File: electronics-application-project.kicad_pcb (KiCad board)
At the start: 2 copper layers, 52 x 32.5 mm, 42 parts, among them J1 Conn_02x03_Odd_Even, U1 W5500, U2 ARJM11C7-114-BA-EW2, U3 LM2574-3.3YN, U4 ATTINY85-20SU, Y2 ABLS7M2-25.000MHZ-D-2Y-T

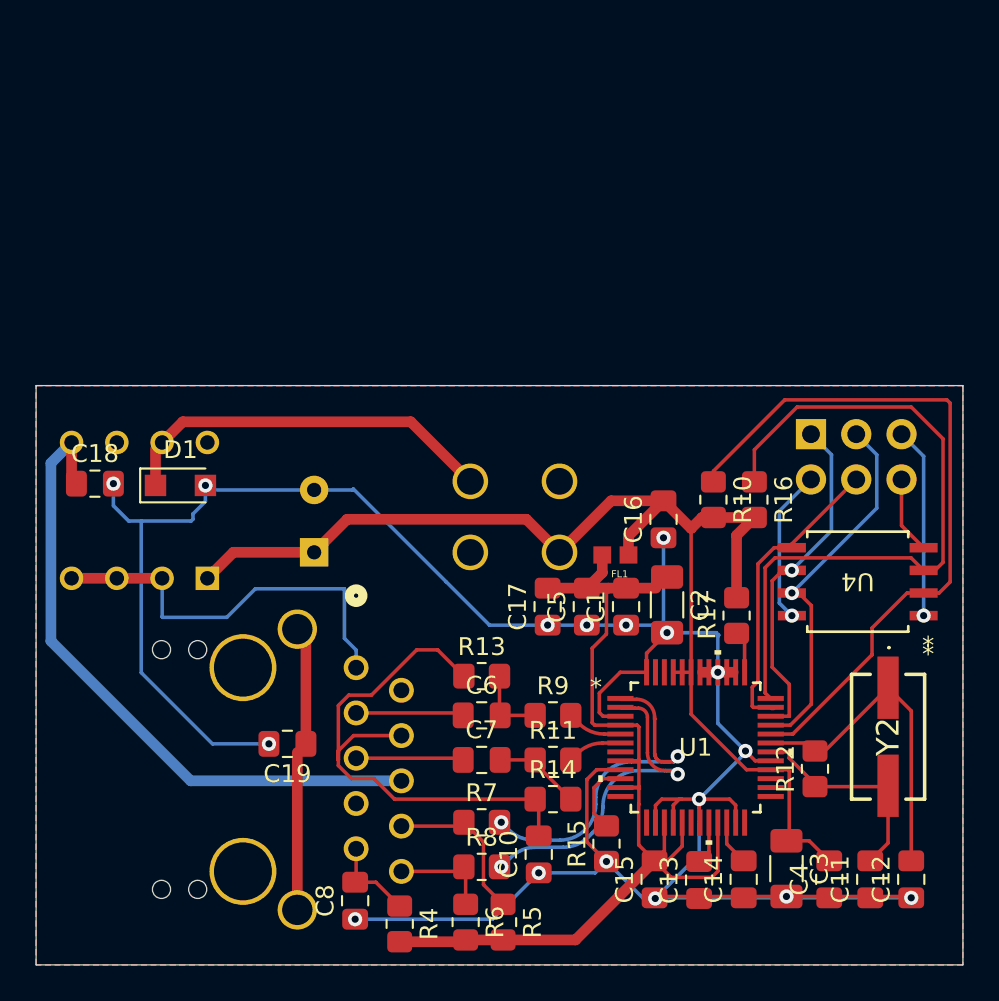
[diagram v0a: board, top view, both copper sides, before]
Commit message: add ethernet leds; change power supply capacitors; change attiny85 pin connections;
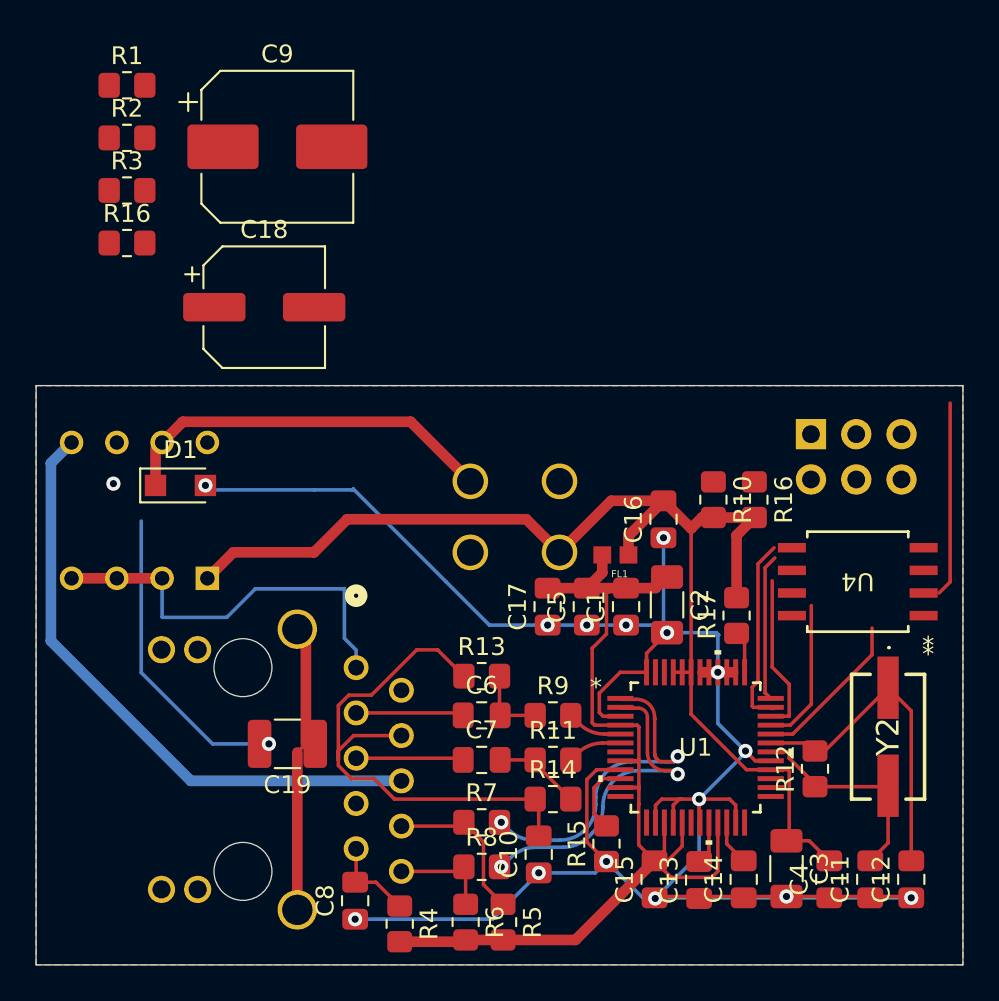
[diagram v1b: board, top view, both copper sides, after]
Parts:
- added R1: 4.7K, Resistor_SMD:R_0805_2012Metric_Pad1.20x1.40mm_HandSolder, F.Cu at (114.6, 54.1)
- added R16: 4.7K, Resistor_SMD:R_0805_2012Metric_Pad1.20x1.40mm_HandSolder, F.Cu at (114.6, 63.0)
- added R2: 330, Resistor_SMD:R_0805_2012Metric_Pad1.20x1.40mm_HandSolder, F.Cu at (114.6, 57.1)
- added R3: 330, Resistor_SMD:R_0805_2012Metric_Pad1.20x1.40mm_HandSolder, F.Cu at (114.6, 60.0)
- C18: footprint Capacitor_SMD:C_0805_2012Metric_Pad1.18x1.45mm_HandSolder -> Capacitor_SMD:CP_Elec_6.3x5.4
- C19: footprint Capacitor_SMD:C_0805_2012Metric_Pad1.18x1.45mm_HandSolder -> Capacitor_SMD:C_1210_3225Metric_Pad1.33x2.70mm_HandSolder
- C9: footprint Capacitor_THT:CP_Radial_D8.0mm_P3.50mm -> Capacitor_SMD:CP_Elec_8x6.2; moved to F.Cu
- U2: footprint Imported:ARJM11C7-114-BA-EW2_ABR -> Imported:ARJM11C7-114-BA-EW2_ABR-fixed
- moved C9 22.8 mm to (123.0, 57.6), turned to 0 degrees
- moved C18 13.7 mm to (122.3, 66.6)
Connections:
- J1 pad 1: /MISO -> /SCLK
- J1 pad 3: /SCLK -> Net-(J1-Pin_3)
- J1 pad 4: /MOSI -> /MISO
- U4 pad 2: /SCSn -> /MOSI
- U4 pad 3: /INTn -> /SCSn
- U4 pad 5: /MOSI -> /MISO
- U4 pad 6: /MISO -> /SCLK
- U4 pad 7: /SCLK -> Net-(J1-Pin_3)
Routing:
- net /SCSn: track 40.1 -> 9.03 mm
- net /INTn: track 39.2 -> 8.24 mm
- net /SCLK: track 21.0 -> 8.30 mm, vias 1 -> 0
- net Net-(J1-Pin_5): track 10.7 -> 0.00 mm, vias 1 -> 0
- net /MISO: track 19.4 -> 9.03 mm, vias 1 -> 0
- net Net-(J1-Pin_2): track 8.67 -> 0.00 mm, vias 1 -> 0
- net GND: track 180.0 -> 171.7 mm
- net /MOSI: track 17.0 -> 21.6 mm
- net Net-(J1-Pin_6): track 4.34 -> 0.00 mm
- net Net-(U2-VC2+): track 37.0 -> 34.5 mm

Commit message: start over
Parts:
- removed the R16 at (114.6, 63.0)
- removed the R16 at (149.8, 77.4)
- added R16: 4.7K, Resistor_SMD:R_0805_2012Metric_Pad1.20x1.40mm_HandSolder, F.Cu at (120.5, 92.7)
- C18, C9, D1: moved to B.Cu
- moved U3 45.4 mm to (161.3, 98.6), turned to 180 degrees
- moved C4 41.5 mm to (131.7, 63.7), turned to 0 degrees
- moved C8 40.2 mm to (136.5, 60.7), turned to 0 degrees
- moved C14 38.8 mm to (141.3, 60.7), turned to 0 degrees
- moved R12 37.9 mm to (115.8, 98.6), turned to 0 degrees
- moved C11 37.6 mm to (136.5, 66.7), turned to 0 degrees
- moved C12 36.4 mm to (136.5, 69.7), turned to 0 degrees
- moved R10 35.2 mm to (115.8, 92.7), turned to 0 degrees
- moved C15 35.1 mm to (141.3, 63.7), turned to 0 degrees
- moved C10 33.6 mm to (136.5, 63.7), turned to 0 degrees
- moved C1 31.4 mm to (148.7, 52.6), turned to 0 degrees
- moved R17 30.6 mm to (120.5, 95.6), turned to 0 degrees
- moved L1 30.6 mm to (122.2, 55.6)
- moved R1 29.9 mm to (111.0, 83.8)
- moved R2 29.9 mm to (111.0, 86.8)
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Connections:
- J1 pad 3: Net-(J1-Pin_3) -> /INTn
- R1 pad 1: Net-(J1-Pin_3) -> /INTn
- U4 pad 7: Net-(J1-Pin_3) -> /INTn
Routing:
- net GND: track 171.7 -> 0.00 mm, vias 17 -> 0
- net 3.3V_D: track 68.8 -> 0.00 mm
- net 3.3V_A: track 60.6 -> 0.00 mm
- net Net-(U2-VC2+): track 34.5 -> 0.00 mm
- net Net-(U2-RCT): track 31.2 -> 0.00 mm
- net Net-(D1-K): track 21.7 -> 0.00 mm
- net /MOSI: track 21.6 -> 0.00 mm
- net Net-(U1-TXN): track 19.1 -> 0.00 mm, vias 2 -> 0
- net Net-(U1-TXP): track 18.7 -> 0.00 mm, vias 2 -> 0
- net /XO: track 18.5 -> 0.00 mm
- net Net-(C19-Pad1): track 17.7 -> 0.00 mm
- net /XI: track 12.3 -> 0.00 mm
- net Net-(U2-TD-): track 9.10 -> 0.00 mm
- net /MISO: track 9.03 -> 0.00 mm
- net /SCSn: track 9.03 -> 0.00 mm
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- removed copper zone on B.Cu, net GND
- removed copper zone on F.Cu, net GND
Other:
- board outline removed

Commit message: pcb progress
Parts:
- R1, R10, R16, R17, R7, R8: moved to B.Cu
- moved R10 80.0 mm to (195.5, 86.0), turned to 90 degrees
- moved C4 77.7 mm to (191.0, 114.0), turned to 90 degrees
- moved C11 75.6 mm to (195.5, 114.0), turned to 90 degrees
- moved C12 75.3 mm to (197.5, 114.0), turned to 90 degrees
- moved R12 75.1 mm to (190.0, 110.0), turned to 90 degrees
- moved R1 75.0 mm to (186.0, 86.0), turned to 90 degrees
- moved C14 73.5 mm to (185.5, 119.5), turned to 90 degrees
- moved R16 70.3 mm to (190.5, 86.0), turned to 90 degrees
- moved C15 67.6 mm to (179.5, 119.5), turned to 90 degrees
- moved Y2 65.3 mm to (194.0, 106.5), turned to -90 degrees
- moved C13 65.2 mm to (182.0, 119.5), turned to 90 degrees
- moved R17 63.2 mm to (183.5, 101.0), turned to 90 degrees
- moved R7 59.4 mm to (170.0, 108.0)
- moved R8 59.0 mm to (170.0, 110.0)
- moved C5 58.7 mm to (177.0, 104.0), turned to 90 degrees
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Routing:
- net GND: track 0.00 -> 44.4 mm, vias 0 -> 1
- net /INTn: track 0.00 -> 36.5 mm
- net /SCSn: track 0.00 -> 33.0 mm, vias 0 -> 1
- net 3.3V_A: track 0.00 -> 31.0 mm
- net /SCLK: track 0.00 -> 25.9 mm
- net /MISO: track 0.00 -> 25.3 mm
- net /XO: track 0.00 -> 23.4 mm
- net /MOSI: track 0.00 -> 19.4 mm, vias 0 -> 2
- net Net-(J1-Pin_5): track 0.00 -> 18.6 mm
- net Net-(J1-Pin_2): track 0.00 -> 15.1 mm
- net 3.3V_D: track 0.00 -> 14.3 mm
- net /XI: track 0.00 -> 13.7 mm
- net Net-(U1-TXP): track 0.00 -> 6.50 mm, vias 0 -> 1
- net Net-(U1-TXN): track 0.00 -> 6.50 mm, vias 0 -> 1
- net Net-(U1-RXP): track 0.00 -> 6.00 mm
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
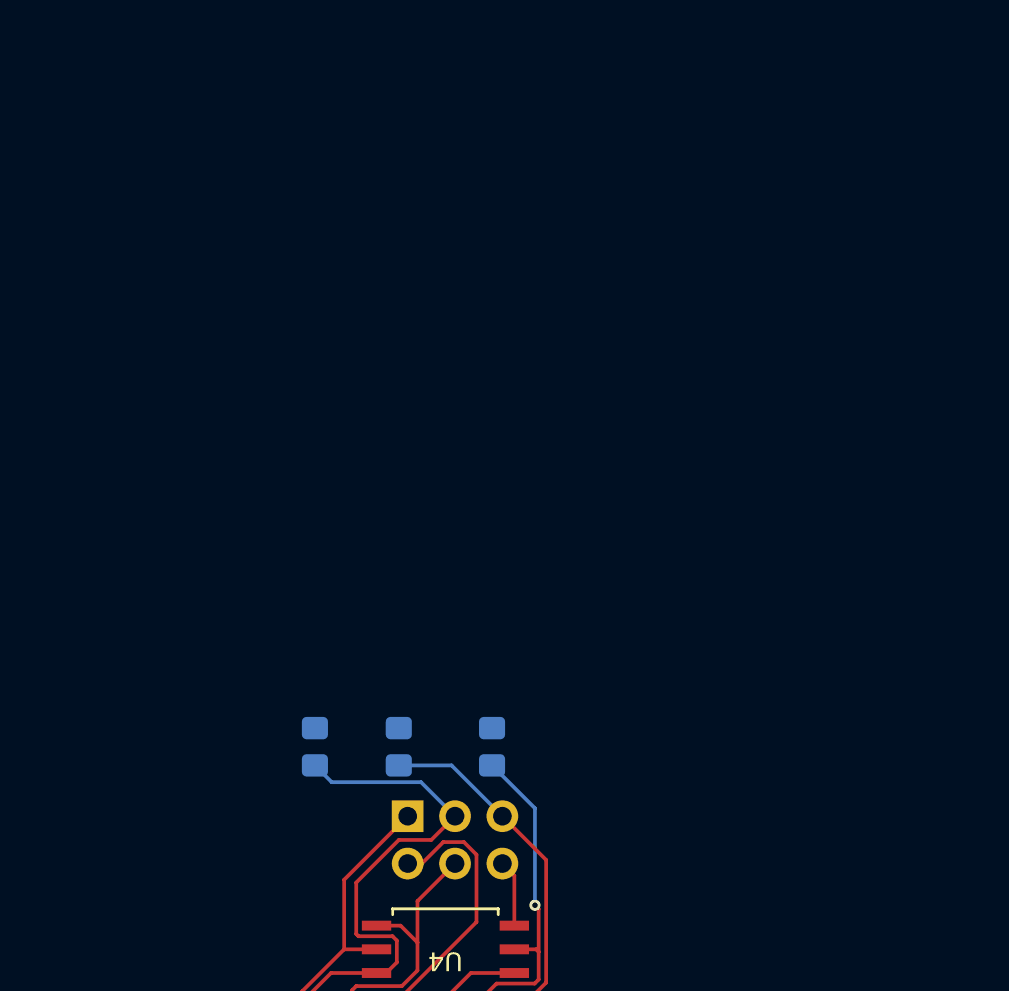
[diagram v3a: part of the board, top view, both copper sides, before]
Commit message: add NAND gates and a pin header for UART and PWM; add buzzer; add pin header for GND and 3.3V_D; expand ATtiny85 pin header to all pins; join W5500 RST and ATtiny85 RST and add a pin header for the net;
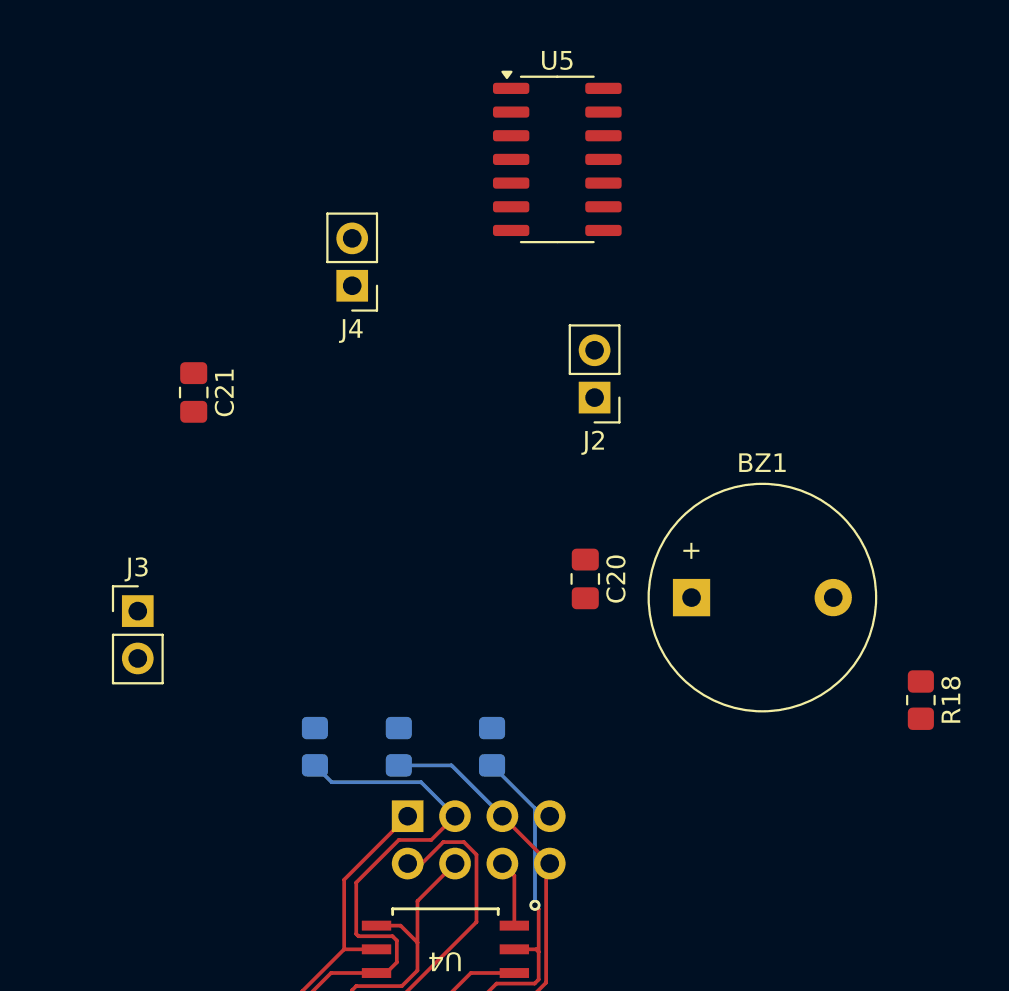
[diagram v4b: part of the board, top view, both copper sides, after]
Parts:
- added BZ1: Buzzer, Buzzer_Beeper:Buzzer_12x9.5RM7.6, F.Cu at (206.2, 78.0)
- added C20: C_Polarized, Capacitor_SMD:C_0805_2012Metric_Pad1.18x1.45mm_HandSolder, F.Cu at (200.5, 77.0)
- added C21: 100nF, Capacitor_SMD:C_0805_2012Metric_Pad1.18x1.45mm_HandSolder, F.Cu at (179.5, 67.0)
- added J2: Conn_01x02_Pin, Connector_PinHeader_2.54mm:PinHeader_1x02_P2.54mm_Vertical, F.Cu at (201.0, 67.3)
- added J3: Conn_01x02_Pin, Connector_PinHeader_2.54mm:PinHeader_1x02_P2.54mm_Vertical, F.Cu at (176.5, 78.7)
- added J4: Conn_01x02_Pin, Connector_PinHeader_2.54mm:PinHeader_1x02_P2.54mm_Vertical, F.Cu at (188.0, 61.3)
- added R18: R, Resistor_SMD:R_0805_2012Metric_Pad1.20x1.40mm_HandSolder, F.Cu at (218.5, 83.5)
- added U5: 74HC00, Package_SO:SO-14_3.9x8.65mm_P1.27mm, F.Cu at (199.0, 54.5)
- J1: footprint Connector_PinHeader_2.54mm:PinHeader_2x03_P2.54mm_Vertical -> Connector_PinHeader_2.54mm:PinHeader_2x04_P2.54mm_Vertical
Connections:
- J1 pad 5: Net-(J1-Pin_5) -> /RSTn
- U4 pad 1: Net-(J1-Pin_5) -> /RSTn

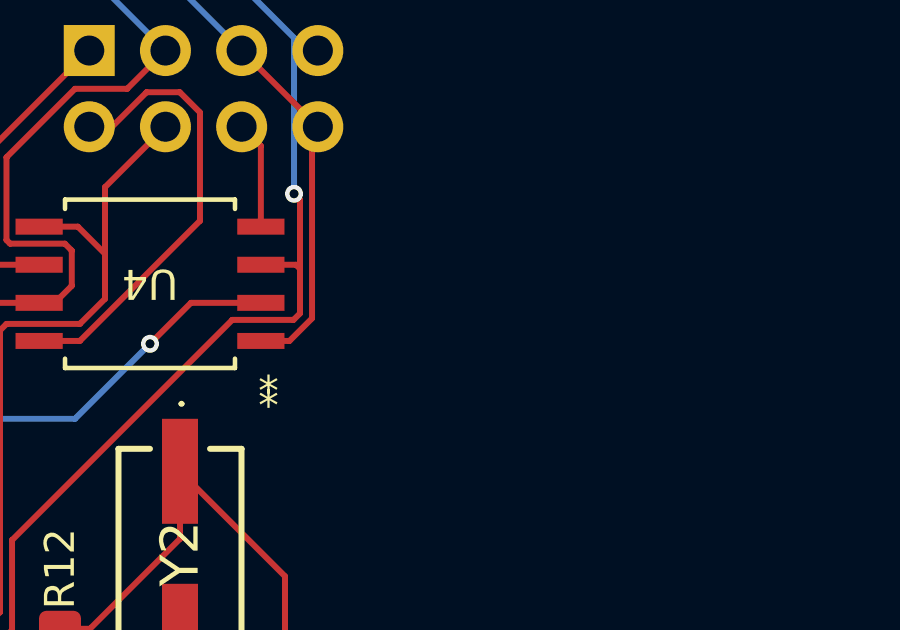
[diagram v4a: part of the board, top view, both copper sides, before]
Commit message: update pcb from schematic
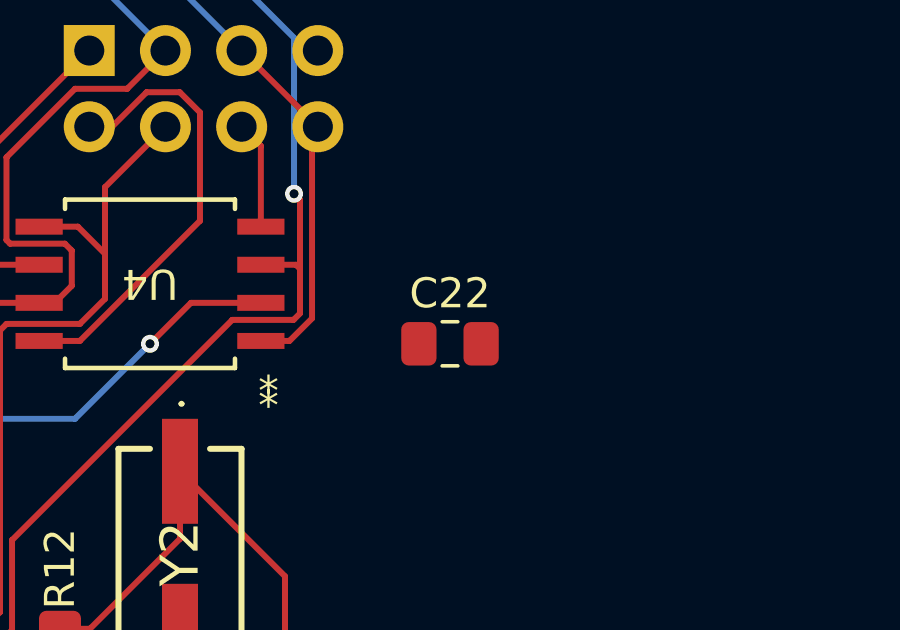
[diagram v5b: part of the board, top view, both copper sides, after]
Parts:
- added C22: C, Capacitor_SMD:C_0805_2012Metric_Pad1.18x1.45mm_HandSolder, F.Cu at (203.0, 99.5)
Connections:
- J1 pad 2: Net-(J1-Pin_2) -> 3.3V_D
- J1 pad 6: Net-(J1-Pin_6) -> GND
- U4 pad 4: Net-(J1-Pin_6) -> GND
- U4 pad 8: Net-(J1-Pin_2) -> 3.3V_D
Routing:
- net Net-(J1-Pin_2): track 15.1 -> 0.00 mm
- net 3.3V_D: track 14.3 -> 29.3 mm
- net GND: track 44.4 -> 48.0 mm
- net Net-(J1-Pin_6): track 3.60 -> 0.00 mm

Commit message: pcb done, but has some errors still
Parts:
- C22, R4, R5, R6: moved to B.Cu
- moved BZ1 61.6 mm to (145.8, 90.0), turned to 180 degrees
- moved C16 59.6 mm to (119.0, 122.0), turned to 90 degrees
- moved C10 58.5 mm to (132.0, 122.0), turned to 90 degrees
- moved C17 55.1 mm to (124.0, 122.0), turned to 90 degrees
- moved U3 52.4 mm to (125.3, 95.3), turned to 90 degrees
- moved R18 50.5 mm to (168.0, 84.5), turned to 0 degrees
- moved J4 46.2 mm to (173.2, 105.0), turned to 90 degrees
- moved U5 45.4 mm to (175.0, 93.0), turned to 180 degrees
- moved C8 45.1 mm to (131.5, 105.5), turned to -90 degrees
- moved C22 43.8 mm to (159.5, 105.0), turned to 90 degrees
- moved R13 41.4 mm to (136.5, 122.0), turned to 90 degrees
- moved R15 41.2 mm to (145.5, 122.5), turned to 90 degrees
- moved R14 40.8 mm to (141.0, 122.0), turned to 90 degrees
- moved L1 40.0 mm to (135.0, 93.5)
- moved D1 35.6 mm to (131.5, 82.0), turned to 0 degrees
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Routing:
- net 3.3V_D: track 29.3 -> 195.2 mm, vias 0 -> 3
- net GND: track 48.0 -> 198.5 mm, vias 1 -> 6
- net 3.3V_A: track 31.0 -> 90.5 mm, vias 0 -> 5
- net /LINK_LED: track 0.00 -> 49.3 mm, vias 0 -> 2
- net /ACT_LED: track 0.00 -> 42.3 mm, vias 0 -> 2
- net /RSTn: track 5.59 -> 47.3 mm
- net Net-(U2-VC2+): track 0.00 -> 37.5 mm
- net Net-(U2-RCT): track 0.00 -> 35.9 mm
- net Net-(BZ1--): track 0.00 -> 31.1 mm
- net Net-(U2-TCT): track 0.00 -> 28.0 mm
- net /SCLK: track 25.9 -> 49.8 mm, vias 0 -> 2
- net /SCSn: track 33.0 -> 55.6 mm
- net Net-(BZ1-+): track 0.00 -> 21.8 mm
- net Net-(J1-Pin_5): track 18.6 -> 0.00 mm
- net Net-(C19-Pad1): track 0.00 -> 17.9 mm
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- added copper zone on B.Cu, net GND
- added copper zone on F.Cu, net GND
